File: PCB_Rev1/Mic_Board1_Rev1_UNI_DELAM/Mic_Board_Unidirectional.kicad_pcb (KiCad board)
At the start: 2 copper layers, 51 x 31.5 mm, 29 parts, among them J2 532610771, J3 S2B-ZR-SM4A-TF_LF__SN_, U1 OPA1671IDBVR

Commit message: Mic Board Setup Changes
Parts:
- moved H4 0.51 mm to (176.1, 94.2)
- moved H2 0.40 mm to (176.1, 69.0)
- moved H3 0.40 mm to (131.3, 94.3)
- moved H1 0.35 mm to (131.3, 69.0)
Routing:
- net GND: track 159.3 -> 188.3 mm
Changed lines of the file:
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@@
 	(footprint "MountingHole:MountingHole_3.2mm_M3_DIN965_Pad"
 		(layer "F.Cu")
-		(at 176.5 69)
+		(at 176.1 69.05)
 		(descr "Mounting Hole 3.2mm, M3, DIN965")
 		(tags "mounting hole 3.2mm m3 din965")
@@
 	(footprint "MountingHole:MountingHole_3.2mm_M3_DIN965_Pad"
 		(layer "F.Cu")
-		(at 131 69)
+		(at 131.35 69.05)
 		(descr "Mounting Hole 3.2mm, M3, DIN965")
 		(tags "mounting hole 3.2mm m3 din965")
@@
 	(footprint "MountingHole:MountingHole_3.2mm_M3_DIN965_Pad"
 		(layer "F.Cu")
-		(at 131 94.5)
+		(at 131.35 94.3)
 		(descr "Mounting Hole 3.2mm, M3, DIN965")
 		(tags "mounting hole 3.2mm m3 din965")
@@
 	(footprint "MountingHole:MountingHole_3.2mm_M3_DIN965_Pad"
 		(layer "F.Cu")
-		(at 176.5 94.5)
+		(at 176.05 94.25)
 		(descr "Mounting Hole 3.2mm, M3, DIN965")
 		(tags "mounting hole 3.2mm m3 din965")
@@
 	)
 	(segment
+		(start 175.636 88.364)
+		(end 176.5 89.228)
+		(width 0.2)
+		(layer "F.Cu")
+		(net 2)
+	)
+	(segment
 		(start 164.68325 81.575004)
 		(end 166.424996 81.575004)
@@
 	)
 	(segment
+		(start 134.180502 94.5)
+		(end 131 94.5)
+		(width 0.2)
+		(layer "F.Cu")
+		(net 2)
+	)
+	(segment
 		(start 136.400002 88.400002)
 		(end 137.2805 89.2805)
@@
 	)
 	(segment
+		(start 175.636 75.175001)
+		(end 175.636 69.864)
+		(width 0.2)
+		(layer "F.Cu")
+		(net 2)
+	)
+	(segment
+		(start 176.5 89.228)
+		(end 176.5 94.5)
+		(width 0.2)
+		(layer "F.Cu")
+		(net 2)
+	)
+	(segment
 		(start 159.1805 69.900002)
 		(end 163.280498 74)
@@
 	)
 	(segment
+		(start 175.636 69.864)
+		(end 176.5 69)
+		(width 0.2)
+		(layer "F.Cu")
+		(net 2)
+	)
+	(segment
 		(start 157.424999 81.575001)
 		(end 158.77775 81.575001)
@@
 	)
 	(segment
+		(start 131 76)
+		(end 131 69)
+		(width 0.2)
+		(layer "F.Cu")
+		(net 2)
+	)
+	(segment
 		(start 155 91.5)
 		(end 155.5 91.5)
@@
 	)
 	(segment
+		(start 137.2805 91.400002)
+		(end 134.180502 94.5)
+		(width 0.2)
+		(layer "F.Cu")
+		(net 2)
+	)
+	(segment
 		(start 164.68325 80.925003)
 		(end 166.574997 80.925003)
@@
 	)
 	(segment
+		(start 130.7805 76.2195)
+		(end 131 76)
+		(width 0.2)
+		(layer "F.Cu")
+		(net 2)
+	)
+	(segment
 		(start 138 77.430502)
 		(end 137.965251 77.465251)
@@
 	)
 	(segment
+		(start 175.636 87.775001)
+		(end 175.636 88.364)
+		(width 0.2)
+		(layer "F.Cu")
+		(net 2)
+	)
+	(segment
 		(start 166.574997 80.925003)
 		(end 167 80.5)
@@
 		(net 2)
 	)
+	(segment
+		(start 130.7805 76.700002)
+		(end 130.7805 76.2195)
+		(width 0.2)
+		(layer "F.Cu")
+		(net 2)
+	)
 	(via
 		(at 149.5 80.5)
@@
 	)
 	(segment
-		(start 155.5 79.5)
-		(end 155.5 83.1)
+		(start 155.4 83.1)
+		(end 155.1 83.4)
 		(width 0.2)
 		(layer "F.Cu")
@@
 	)
 	(segment
-		(start 155.5 83.1)
-		(end 155.1 83.5)
-		(width 0.2)
-		(layer "F.Cu")
-		(net 8)
-	)
-	(segment
 		(start 142.5 78.1)
 		(end 142.5 71)
@@
 	)
 	(segment
-		(start 155.1 86.5)
-		(end 155.1 87.4)
-		(width 0.2)
-		(layer "F.Cu")
-		(net 8)
-	)
-	(segment
-		(start 171.725001 80.225001)
-		(end 171.5 80)
-		(width 0.2)
-		(layer "F.Cu")
-		(net 8)
-	)
-	(segment
-		(start 172.736 80.225001)
-		(end 171.725001 80.225001)
-		(width 0.2)
-		(layer "F.Cu")
-		(net 8)
-	)
-	(segment
 		(start 142 70.5)
 		(end 139.9125 70.5)
@@
 	)
 	(segment
+		(start 171.725001 80.225001)
+		(end 172.736 80.225001)
+		(width 0.2)
+		(layer "F.Cu")
+		(net 8)
+	)
+	(segment
 		(start 158.77775 82.225)
 		(end 158.77775 82.875001)
@@
 	)
 	(segment
+		(start 155.5 83)
+		(end 155.5 79.5)
+		(width 0.2)
+		(layer "F.Cu")
+		(net 8)
+	)
+	(segment
 		(start 158.77775 82.225)
 		(end 157.775 82.225)
@@
 	)
 	(segment
-		(start 155.1 83.5)
-		(end 155.1 86.5)
+		(start 153.2305 78.2305)
+		(end 153 78)
 		(width 0.2)
 		(layer "F.Cu")
@@
 	)
 	(segment
-		(start 153.2305 78.2305)
-		(end 153 78)
+		(start 155.1 83.4)
+		(end 155.1 87.4)
 		(width 0.2)
 		(layer "F.Cu")
@@
 	)
 	(segment
+		(start 155.4 83.1)
+		(end 155.5 83)
+		(width 0.2)
+		(layer "F.Cu")
+		(net 8)
+	)
+	(segment
 		(start 155 87.5)
 		(end 155.1 87.4)
@@
 		(net 8)
 	)
+	(segment
+		(start 171 79.5)
+		(end 171.725001 80.225001)
+		(width 0.2)
+		(layer "F.Cu")
+		(net 8)
+	)
 	(via
 		(at 155.1 87.4)
@@
 	)
 	(via
-		(at 171.5 80)
+		(at 171 79.5)
 		(size 0.6)
 		(drill 0.3)
@@
 	)
 	(via
-		(at 155.1 83.5)
+		(at 155.4 83.1)
 		(size 0.6)
 		(drill 0.3)
@@
 	)
 	(segment
+		(start 155.5 83)
+		(end 157 83)
+		(width 0.2)
+		(layer "B.Cu")
+		(net 8)
+	)
+	(segment
 		(start 163 88.5)
 		(end 161 88.5)
@@
 	)
 	(segment
-		(start 153 78)
-		(end 152.9 78.1)
+		(start 155.4 83.1)
+		(end 155.5 83)
 		(width 0.2)
 		(layer "B.Cu")
@@
 	)
 	(segment
-		(start 155.6 83)
-		(end 155.1 83.5)
+		(start 153 78)
+		(end 152.9 78.1)
 		(width 0.2)
 		(layer "B.Cu")
@@
 	)
 	(segment
-		(start 157 83)
-		(end 155.6 83)
-		(width 0.2)
-		(layer "B.Cu")
-		(net 8)
-	)
-	(segment
 		(start 171 79.5)
 		(end 168 79.5)
@@
 	)
 	(segment
-		(start 171.5 80)
-		(end 171 79.5)
-		(width 0.2)
-		(layer "B.Cu")
-		(net 8)
-	)
-	(segment
 		(start 156.2 78.5)
 		(end 156.2 79.6)
@@
 	)
 	(segment
-		(start 172.510999 82.5)
-		(end 172.736 82.725001)
+		(start 170.81907 82.776749)
+		(end 170.870818 82.725001)
 		(width 0.2)
 		(layer "F.Cu")
@@
 	)
 	(segment
-		(start 171.5 82.5)
-		(end 172.510999 82.5)
+		(start 164.68325 82.875001)
+		(end 165.755352 82.875001)
 		(width 0.2)
 		(layer "F.Cu")
@@
 	)
 	(segment
-		(start 164.68325 82.875001)
-		(end 165.755352 82.875001)
+		(start 170.870818 82.725001)
+		(end 172.736 82.725001)
 		(width 0.2)
 		(layer "F.Cu")
@@
 	)
 	(via
-		(at 171.5 82.5)
+		(at 170.81907 82.776749)
 		(size 0.6)
 		(drill 0.3)
@@
 	)
 	(segment
-		(start 166.120261 83)
-		(end 171 83)
+		(start 170.81907 82.776749)
+		(end 170.595819 83)
 		(width 0.2)
 		(layer "B.Cu")
@@
 	)
 	(segment
-		(start 166.000306 83.119955)
+		(start 170.595819 83)
 		(end 166.120261 83)
 		(width 0.2)
@@
 	)
 	(segment
-		(start 171 83)
-		(end 171.5 82.5)
+		(start 166.120261 83)
+		(end 166.000306 83.119955)
 		(width 0.2)
 		(layer "B.Cu")
@@
 	)
 	(segment
-		(start 171.5 83.5)
-		(end 172.260999 83.5)
+		(start 172.680956 83.919957)
+		(end 172.736 83.975001)
 		(width 0.2)
 		(layer "F.Cu")
@@
 	)
 	(segment
-		(start 172.260999 83.5)
-		(end 172.736 83.975001)
+		(start 170.5 83.919957)
+		(end 172.680956 83.919957)
 		(width 0.2)
 		(layer "F.Cu")
@@
 	)
 	(via
-		(at 171.5 83.5)
+		(at 170.5 83.919957)
 		(size 0.6)
 		(drill 0.3)
@@
 	)
 	(segment
-		(start 171.080043 83.919957)
-		(end 171.5 83.5)
-		(width 0.2)
-		(layer "B.Cu")
-		(net 16)
-	)
-	(segment
-		(start 165.999662 83.919957)
-		(end 171.080043 83.919957)
+		(start 170.5 83.919957)
+		(end 165.999662 83.919957)
 		(width 0.2)
 		(layer "B.Cu")

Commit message: Micboard Changes
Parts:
- moved R7 5.69 mm to (164.6, 70.5)
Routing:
- net GND: track 188.3 -> 172.0 mm, vias 16 -> 15
- net Net-(U2-CKS): track 5.81 -> 2.94 mm
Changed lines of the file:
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@@
 	(footprint "Resistor_SMD:R_0805_2012Metric"
 		(layer "F.Cu")
-		(at 166.318 75.900002)
+		(at 164.618 70.4695)
 		(descr "Resistor SMD 0805 (2012 Metric), square (rectangular) end terminal, IPC_7351 nominal, (Body size source: IPC-SM-782 page 72, https://www.pcb-3d.com/wordpress/wp-content/uploads/ipc-sm-782a_amendment_1_and_2.pdf), generated with kicad-footprint-generator")
 		(tags "resistor")
@@
 	)
 	(segment
-		(start 165.4055 74.4055)
-		(end 165.4055 75.900002)
-		(width 0.2)
-		(layer "F.Cu")
-		(net 2)
-	)
-	(segment
 		(start 175.636 88.364)
 		(end 176.5 89.228)
@@
 	)
 	(segment
-		(start 163.280498 74)
-		(end 165 74)
-		(width 0.2)
-		(layer "F.Cu")
-		(net 2)
-	)
-	(segment
 		(start 156 92)
 		(end 156 93.900002)
@@
 	)
 	(segment
-		(start 159.1805 69.900002)
-		(end 163.280498 74)
-		(width 0.2)
-		(layer "F.Cu")
-		(net 2)
-	)
-	(segment
 		(start 130.7805 79.2805)
 		(end 130.7805 76.700002)
@@
 	)
 	(segment
-		(start 165 74)
-		(end 165.4055 74.4055)
-		(width 0.2)
-		(layer "F.Cu")
-		(net 2)
-	)
-	(segment
 		(start 135.2805 80.150002)
 		(end 134.3805 80.150002)
@@
 	)
 	(via
-		(at 165 74)
-		(size 0.6)
-		(drill 0.3)
-		(layers "F.Cu" "B.Cu")
-		(net 2)
-	)
-	(via
 		(at 173.275001 87.775001)
 		(size 0.6)
@@
 	)
 	(segment
-		(start 171.5 73.5)
-		(end 165.5 73.5)
-		(width 0.2)
-		(layer "B.Cu")
-		(net 2)
-	)
-	(segment
 		(start 145.5 80)
 		(end 146 80.5)
@@
 	)
 	(segment
-		(start 165.5 73.5)
-		(end 165 74)
-		(width 0.2)
-		(layer "B.Cu")
-		(net 2)
-	)
-	(segment
 		(start 158.5 92)
 		(end 156 92)
@@
 	)
 	(segment
-		(start 167.2305 75.900002)
-		(end 167.2 75.930502)
+		(start 165.5305 70.4695)
+		(end 165.5 70.5)
 		(width 0.2)
 		(layer "F.Cu")
@@
 		(width 0.2)
 		(layer "F.Cu")
-		(net 13)
-	)
-	(segment
-		(start 167.2305 78.7695)
-		(end 167.2305 75.900002)
-		(width 0.2)
-		(layer "F.Cu")

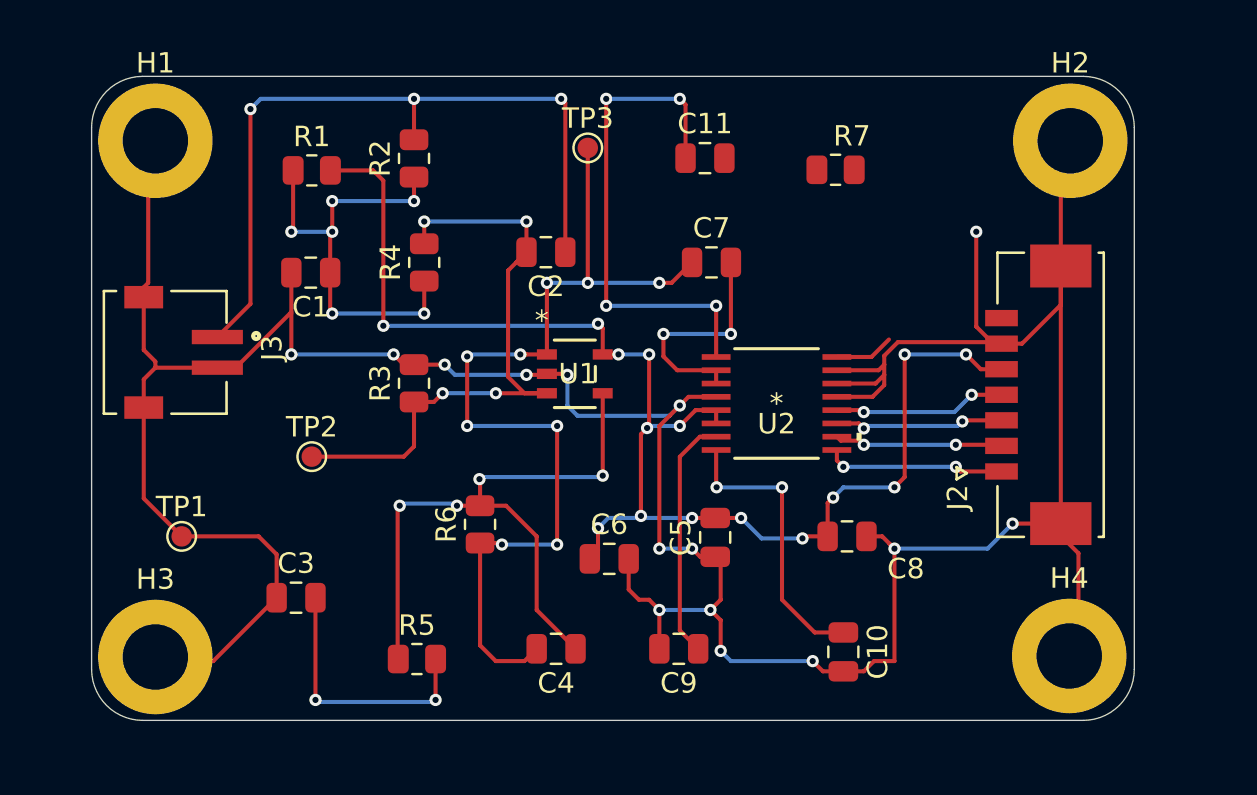
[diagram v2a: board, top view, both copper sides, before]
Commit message: MicBoard silkscreen updated
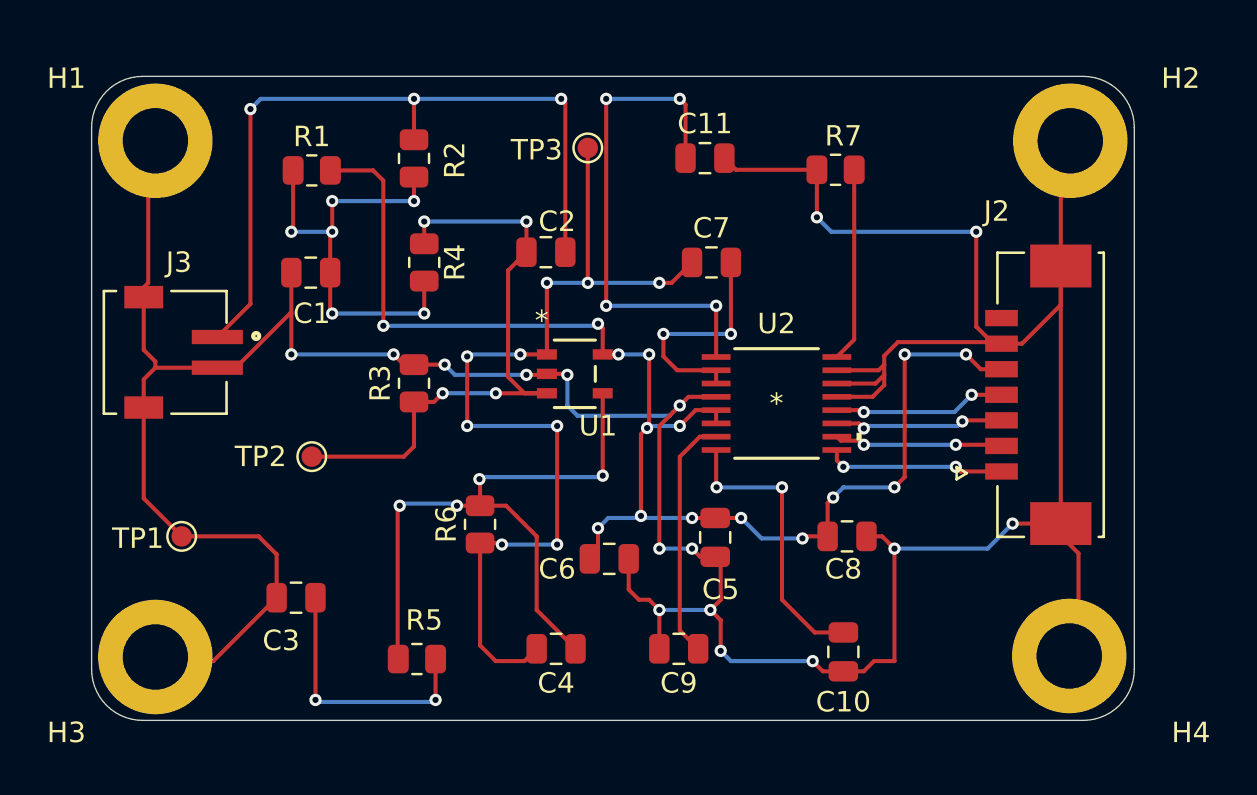
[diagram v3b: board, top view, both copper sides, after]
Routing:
- net GND: track 172.0 -> 187.2 mm, vias 15 -> 16
- net Net-(U2-CKS): track 2.94 -> 9.55 mm
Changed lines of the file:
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@@
 		(tags "AK5720VT ")
 		(property "Reference" "U2"
-			(at 0 1 0)
+			(at 0 -3.900002 0)
 			(unlocked yes)
 			(layer "F.SilkS")
@@
 		(tags "capacitor")
 		(property "Reference" "C5"
-			(at 0 -1.68 90)
+			(at -2.549998 0.2695 180)
 			(layer "F.SilkS")
 			(effects
@@
 		(tags "test point SMD pad")
 		(property "Reference" "TP1"
-			(at 0 -1.448 0)
+			(at -2.136 0.099998 0)
 			(layer "F.SilkS")
 			(effects
@@
 		(at 132.2305 79.400002 -90)
 		(property "Reference" "J3"
-			(at -0.215 -4.825 90)
+			(at -4.400002 -0.2695 180)
 			(layer "F.SilkS")
 			(effects
@@
 		(tags "resistor")
 		(property "Reference" "R5"
-			(at 0 -1.65 0)
+			(at 0.357 -1.900002 0)
 			(layer "F.SilkS")
 			(effects
@@
 		(tags "resistor")
 		(property "Reference" "R4"
-			(at 0 -1.65 90)
+			(at 0 1.5 -90)
 			(layer "F.SilkS")
 			(effects
@@
 		(tags "OPA1671IDBVR ")
 		(property "Reference" "U1"
-			(at 0.13475 0 0)
+			(at 1.13475 2.549999 0)
 			(unlocked yes)
 			(layer "F.SilkS")
@@
 		(tags "capacitor")
 		(property "Reference" "C10"
-			(at 0 -1.68 90)
+			(at 2.45 0 180)
 			(layer "F.SilkS")
 			(effects
@@
 		(tags "resistor")
 		(property "Reference" "R7"
-			(at 0.8 -1.65 0)
+			(at 0.382 -1.65 0)
 			(layer "F.SilkS")
 			(effects
@@
 		(tags "capacitor")
 		(property "Reference" "C3"
-			(at 0 -1.68 0)
+			(at -0.7305 2.099998 0)
 			(layer "F.SilkS")
 			(effects
@@
 		(tags "test point SMD pad")
 		(property "Reference" "TP2"
-			(at 0 -1.448 0)
+			(at -2.5 0 0)
 			(layer "F.SilkS")
 			(effects
@@
 		(tags "mounting hole 3.2mm m3 din965")
 		(property "Reference" "H2"
-			(at 0 -3.8 0)
+			(at 5.4 -3.05 0)
 			(layer "F.SilkS")
 			(effects
@@
 		(tags "capacitor")
 		(property "Reference" "C8"
-			(at -2.874999 -1.5855 0)
+			(at 0.1805 -1.599998 0)
 			(layer "F.SilkS")
 			(effects
@@
 		(tags "capacitor")
 		(property "Reference" "C6"
-			(at 0 -1.68 0)
+			(at -2.55 0.5 0)
 			(layer "F.SilkS")
 			(effects
@@
 		(at 175.136 81.475001 90)
 		(property "Reference" "J2"
-			(at -5.025 -4.543 90)
+			(at 8.975001 -2.636 180)
 			(layer "F.SilkS")
 			(effects
@@
 		(tags "mounting hole 3.2mm m3 din965")
 		(property "Reference" "H1"
-			(at 0 -3.8 0)
+			(at -4.35 -3.05 0)
 			(layer "F.SilkS")
 			(effects
@@
 		(tags "mounting hole 3.2mm m3 din965")
 		(property "Reference" "H3"
-			(at 0 -3.8 0)
+			(at -4.35 3.7 0)
 			(layer "F.SilkS")
 			(effects
@@
 		(tags "resistor")
 		(property "Reference" "R2"
-			(at 0 -1.65 90)
+			(at -0.0875 2 -90)
 			(layer "F.SilkS")
 			(effects
@@
 		(tags "mounting hole 3.2mm m3 din965")
 		(property "Reference" "H4"
-			(at 0 -3.8 0)
+			(at 5.95 3.75 0)
 			(layer "F.SilkS")
 			(effects
@@
 		(tags "capacitor")
 		(property "Reference" "C2"
-			(at 0 -1.68 0)
+			(at -0.55 1.5 0)
 			(layer "F.SilkS")
 			(effects
@@
 		(tags "test point SMD pad")
 		(property "Reference" "TP3"
-			(at 0 -1.448 0)
+			(at -2.5 0.099998 0)
 			(layer "F.SilkS")
 			(effects
@@
 		(tags "capacitor")
 		(property "Reference" "C1"
-			(at 0 -1.68 0)
+			(at -0.05 -2 0)
 			(layer "F.SilkS")
 			(effects
@@
 	)
 	(segment
+		(start 159.1805 69.900002)
+		(end 159.749998 70.4695)
+		(width 0.2)
+		(layer "F.Cu")
+		(net 2)
+	)
+	(segment
 		(start 165 95)
 		(end 164 95)
@@
 	)
 	(segment
+		(start 159.749998 70.4695)
+		(end 163.7055 70.4695)
+		(width 0.2)
+		(layer "F.Cu")
+		(net 2)
+	)
+	(segment
 		(start 172.736 78.975001)
 		(end 172.336 78.975001)
@@
 	)
 	(segment
+		(start 163.7055 72.7945)
+		(end 163.7055 70.4695)
+		(width 0.2)
+		(layer "F.Cu")
+		(net 2)
+	)
+	(segment
 		(start 167.665686 78.9)
 		(end 172.660999 78.9)
@@
 	)
 	(via
+		(at 163.7055 72.7945)
+		(size 0.6)
+		(drill 0.3)
+		(layers "F.Cu" "B.Cu")
+		(net 2)
+	)
+	(via
 		(at 156 89)
 		(size 0.6)
@@
 	)
 	(segment
+		(start 164.411 73.5)
+		(end 163.7055 72.7945)
+		(width 0.2)
+		(layer "B.Cu")
+		(net 2)
+	)
+	(segment
 		(start 172.050002 89)
 		(end 173.275001 87.775001)
@@
 	)
 	(segment
+		(start 171.5 73.5)
+		(end 164.411 73.5)
+		(width 0.2)
+		(layer "B.Cu")
+		(net 2)
+	)
+	(segment
 		(start 158.5 92)
 		(end 156 92)
@@
 	)
 	(segment
-		(start 164.68325 79.625003)
-		(end 166.374997 79.625003)
+		(start 165.5305 70.4695)
+		(end 165.5305 78.777753)
 		(width 0.2)
 		(layer "F.Cu")
@@
 	)
 	(segment
-		(start 166.374997 79.625003)
-		(end 167.2305 78.7695)
+		(start 165.5305 78.777753)
+		(end 164.68325 79.625003)
 		(width 0.2)
 		(layer "F.Cu")

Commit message: more MicBoard re-routing
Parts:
- moved R7 6.31 mm to (168.4, 75.5), turned to 180 degrees
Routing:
- net Net-(U2-CKS): track 9.55 -> 5.29 mm
- net GND: track 187.2 -> 190.2 mm
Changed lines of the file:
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@@
 	(footprint "Resistor_SMD:R_0805_2012Metric"
 		(layer "F.Cu")
-		(at 164.618 70.4695)
+		(at 168.382 75.5305 180)
 		(descr "Resistor SMD 0805 (2012 Metric), square (rectangular) end terminal, IPC_7351 nominal, (Body size source: IPC-SM-782 page 72, https://www.pcb-3d.com/wordpress/wp-content/uploads/ipc-sm-782a_amendment_1_and_2.pdf), generated with kicad-footprint-generator")
 		(tags "resistor")
 		(property "Reference" "R7"
-			(at 0.382 -1.65 0)
+			(at 0.382 -1.65 360)
 			(layer "F.SilkS")
 			(effects
@@
 		)
 		(property "Value" "1k"
-			(at 0 1.65 0)
+			(at 0 1.65 360)
 			(layer "F.Fab")
 			(effects
@@
 		)
 		(property "Footprint" "Resistor_SMD:R_0805_2012Metric"
-			(at 0 0 0)
+			(at 0 0 180)
 			(unlocked yes)
 			(layer "F.Fab")
@@
 		)
 		(property "Datasheet" ""
-			(at 0 0 0)
+			(at 0 0 180)
 			(unlocked yes)
 			(layer "F.Fab")
@@
 		)
 		(property "Description" ""
-			(at 0 0 0)
+			(at 0 0 180)
 			(unlocked yes)
 			(layer "F.Fab")
@@
 		(attr smd)
 		(fp_line
-			(start -0.227064 -0.735)
-			(end 0.227064 -0.735)
+			(start -0.227064 0.735)
+			(end 0.227064 0.735)
 			(stroke
 				(width 0.12)
@@
 		)
 		(fp_line
-			(start -0.227064 0.735)
-			(end 0.227064 0.735)
+			(start -0.227064 -0.735)
+			(end 0.227064 -0.735)
 			(stroke
 				(width 0.12)
@@
 		)
 		(fp_line
-			(start -1.68 -0.95)
-			(end 1.68 -0.95)
+			(start 1.68 0.95)
+			(end -1.68 0.95)
 			(stroke
 				(width 0.05)
@@
 		)
 		(fp_line
-			(start -1.68 0.95)
-			(end -1.68 -0.95)
+			(start 1.68 -0.95)
+			(end 1.68 0.95)
 			(stroke
 				(width 0.05)
@@
 		)
 		(fp_line
-			(start 1.68 -0.95)
-			(end 1.68 0.95)
+			(start -1.68 0.95)
+			(end -1.68 -0.95)
 			(stroke
 				(width 0.05)
@@
 		)
 		(fp_line
-			(start 1.68 0.95)
-			(end -1.68 0.95)
+			(start -1.68 -0.95)
+			(end 1.68 -0.95)
 			(stroke
 				(width 0.05)
@@
 		)
 		(fp_line
-			(start -1 -0.625)
-			(end 1 -0.625)
+			(start 1 0.625)
+			(end -1 0.625)
 			(stroke
 				(width 0.1)
@@
 		)
 		(fp_line
-			(start -1 0.625)
-			(end -1 -0.625)
+			(start 1 -0.625)
+			(end 1 0.625)
 			(stroke
 				(width 0.1)
@@
 		)
 		(fp_line
-			(start 1 -0.625)
-			(end 1 0.625)
+			(start -1 0.625)
+			(end -1 -0.625)
 			(stroke
 				(width 0.1)
@@
 		)
 		(fp_line
-			(start 1 0.625)
-			(end -1 0.625)
+			(start -1 -0.625)
+			(end 1 -0.625)
 			(stroke
 				(width 0.1)
@@
 		)
 		(fp_text user "${REFERENCE}"
-			(at 0 0 0)
+			(at 0 0 360)
 			(layer "F.Fab")
 			(effects
@@
 		)
 		(pad "1" smd roundrect
-			(at -0.9125 0)
+			(at -0.9125 0 180)
 			(size 1.025 1.4)
 			(layers "F.Cu" "F.Paste" "F.Mask")
@@
 		)
 		(pad "2" smd roundrect
-			(at 0.9125 0)
+			(at 0.9125 0 180)
 			(size 1.025 1.4)
 			(layers "F.Cu" "F.Paste" "F.Mask")
@@
 		(tags "capacitor")
 		(property "Reference" "C11"
-			(at 0 -1.68 0)
+			(at 0.7695 -1.68 0)
 			(layer "F.SilkS")
 			(effects
@@
 	)
 	(segment
-		(start 159.1805 69.900002)
-		(end 159.749998 70.4695)
-		(width 0.2)
-		(layer "F.Cu")
-		(net 2)
-	)
-	(segment
 		(start 165 95)
 		(end 164 95)
@@
 	)
 	(segment
+		(start 159.1805 72.1805)
+		(end 160.5 73.5)
+		(width 0.2)
+		(layer "F.Cu")
+		(net 2)
+	)
+	(segment
 		(start 173.275001 87.775001)
 		(end 175.636 87.775001)
@@
 	)
 	(segment
-		(start 159.749998 70.4695)
-		(end 163.7055 70.4695)
+		(start 159.1805 69.900002)
+		(end 159.1805 72.1805)
 		(width 0.2)
 		(layer "F.Cu")
@@
 	)
 	(segment
+		(start 171.5 73.5)
+		(end 169.4695 75.5305)
+		(width 0.2)
+		(layer "F.Cu")
+		(net 2)
+	)
+	(segment
 		(start 138 77.5)
 		(end 137.965251 77.465251)
@@
 	)
 	(segment
+		(start 169.4695 75.5305)
+		(end 169.2945 75.5305)
+		(width 0.2)
+		(layer "F.Cu")
+		(net 2)
+	)
+	(segment
 		(start 166.424996 81.575004)
 		(end 167 81)
@@
 	)
 	(segment
-		(start 163.7055 72.7945)
-		(end 163.7055 70.4695)
-		(width 0.2)
-		(layer "F.Cu")
-		(net 2)
-	)
-	(segment
 		(start 167.665686 78.9)
 		(end 172.660999 78.9)
@@
 	)
 	(via
-		(at 163.7055 72.7945)
+		(at 160.5 73.5)
 		(size 0.6)
 		(drill 0.3)
@@
 	)
 	(segment
-		(start 164.411 73.5)
-		(end 163.7055 72.7945)
-		(width 0.2)
-		(layer "B.Cu")
-		(net 2)
-	)
-	(segment
 		(start 172.050002 89)
 		(end 173.275001 87.775001)
@@
 	)
 	(segment
-		(start 145.5 80)
-		(end 146 80.5)
+		(start 160.5 73.5)
+		(end 171.5 73.5)
 		(width 0.2)
 		(layer "B.Cu")
@@
 	)
 	(segment
-		(start 171.5 73.5)
-		(end 164.411 73.5)
+		(start 145.5 80)
+		(end 146 80.5)
 		(width 0.2)
 		(layer "B.Cu")
@@
 	)
 	(segment
-		(start 165.5305 70.4695)
-		(end 165.5 70.5)
+		(start 167.4695 75.5305)
+		(end 167.5 75.5)
 		(width 0.2)
 		(layer "F.Cu")
@@
 	)
 	(segment
-		(start 165.5305 70.4695)
-		(end 165.5305 78.777753)
+		(start 164.68325 78.31675)
+		(end 167.4695 75.5305)
 		(width 0.2)
 		(layer "F.Cu")
@@
 	)
 	(segment
-		(start 165.5305 78.777753)
-		(end 164.68325 79.625003)
+		(start 164.68325 79.625003)
+		(end 164.68325 78.31675)
 		(width 0.2)
 		(layer "F.Cu")
